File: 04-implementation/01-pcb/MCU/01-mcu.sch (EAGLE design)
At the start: 49 parts, among them IC1 PIC24FJ128GB204, J2 ARDUINO-CONN-8X2, J3 ARDUINO-CONN-8X2, J4 ARDUINO-CONN-8, J6 ARDUINO-CONN-6, J7 PICKIT-ICSP, U2 ICE40-HX1K-VQFP100, U3 SP0502BAHT-SOT23, U4 MCP1700-SOT89, U6 MCP1700-SOT89

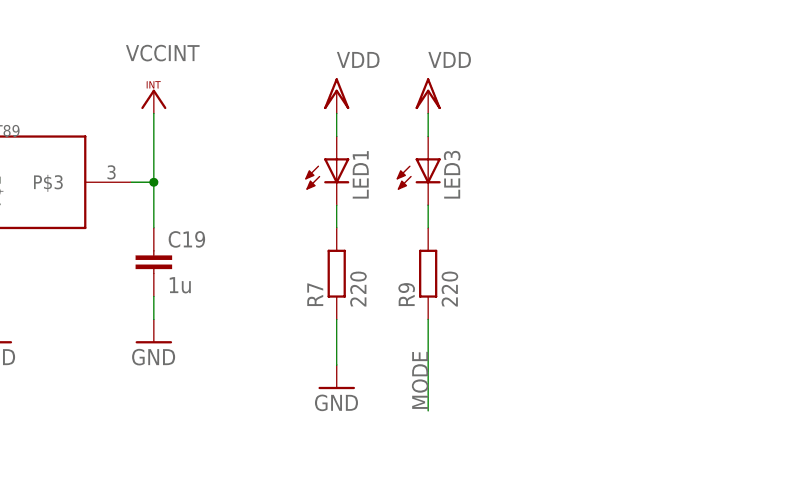
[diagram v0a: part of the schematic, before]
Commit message: Add files to release PCB after successful board bring up.
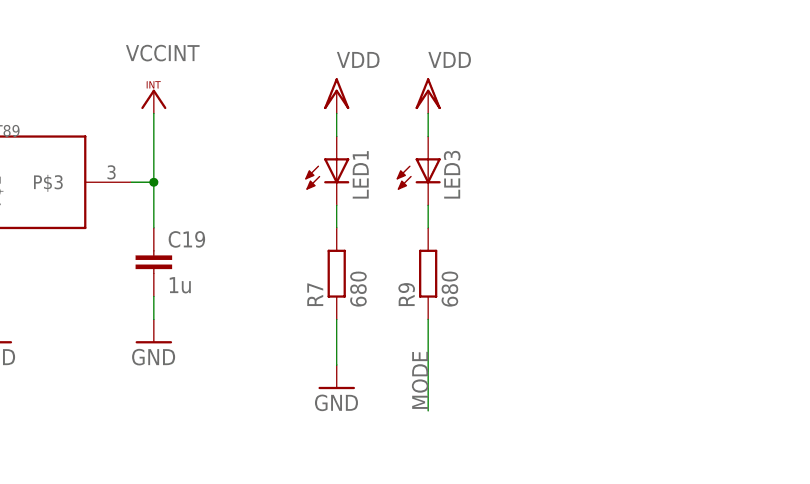
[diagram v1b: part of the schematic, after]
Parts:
- R7, R9: value 220 -> 680
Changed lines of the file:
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@@
 <?xml version="1.0" encoding="utf-8"?>
 <!DOCTYPE eagle SYSTEM "eagle.dtd">
-<eagle version="8.7.1">
+<eagle version="9.0.0">
 <drawing>
 <settings>
@@
 <part name="VDD26" library="supply1" library_urn="urn:adsk.eagle:library:371" deviceset="VDD" device=""/>
 <part name="LED1" library="MIDI router MCU parts" deviceset="LED" device="CHIP-LED0805"/>
-<part name="R7" library="rcl" library_urn="urn:adsk.eagle:library:334" deviceset="R-EU_" device="R0805" package3d_urn="urn:adsk.eagle:package:23553/2" value="220"/>
+<part name="R7" library="rcl" library_urn="urn:adsk.eagle:library:334" deviceset="R-EU_" device="R0805" package3d_urn="urn:adsk.eagle:package:23553/2" value="680"/>
 <part name="GND36" library="supply1" library_urn="urn:adsk.eagle:library:371" deviceset="GND" device=""/>
 <part name="LED3" library="MIDI router MCU parts" deviceset="LED" device="CHIP-LED0805"/>
-<part name="R9" library="rcl" library_urn="urn:adsk.eagle:library:334" deviceset="R-EU_" device="R0805" package3d_urn="urn:adsk.eagle:package:23553/2" value="220"/>
+<part name="R9" library="rcl" library_urn="urn:adsk.eagle:library:334" deviceset="R-EU_" device="R0805" package3d_urn="urn:adsk.eagle:package:23553/2" value="680"/>
 <part name="VDD27" library="supply1" library_urn="urn:adsk.eagle:library:371" deviceset="VDD" device=""/>
 <part name="U6" library="MIDI router MCU parts" deviceset="MCP1700-SOT89" device=""/>
